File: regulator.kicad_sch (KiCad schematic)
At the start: 23 parts, among them U4 TPS63020DSJR, U5 MD53R33

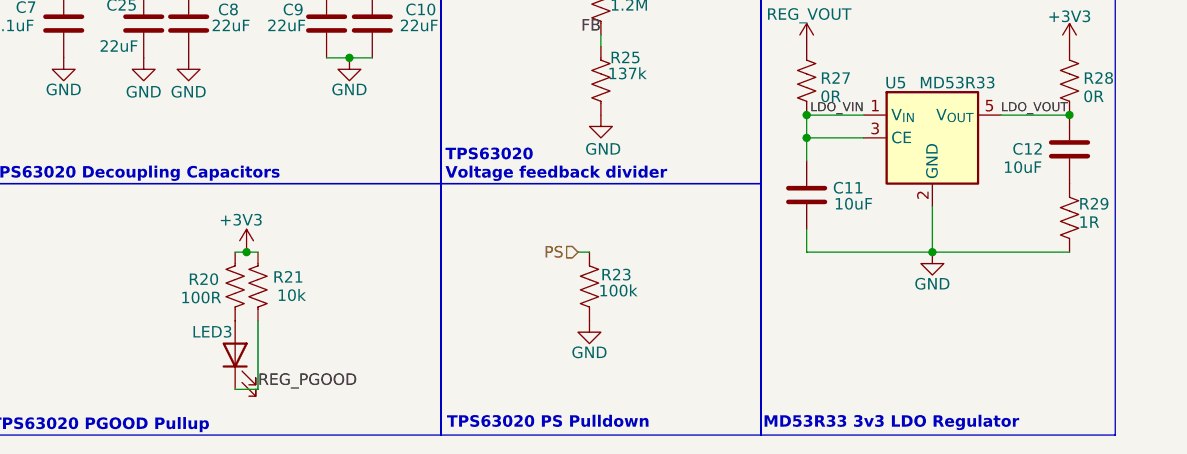
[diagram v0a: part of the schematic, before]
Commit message: Added labels and schematic PDF among other progress
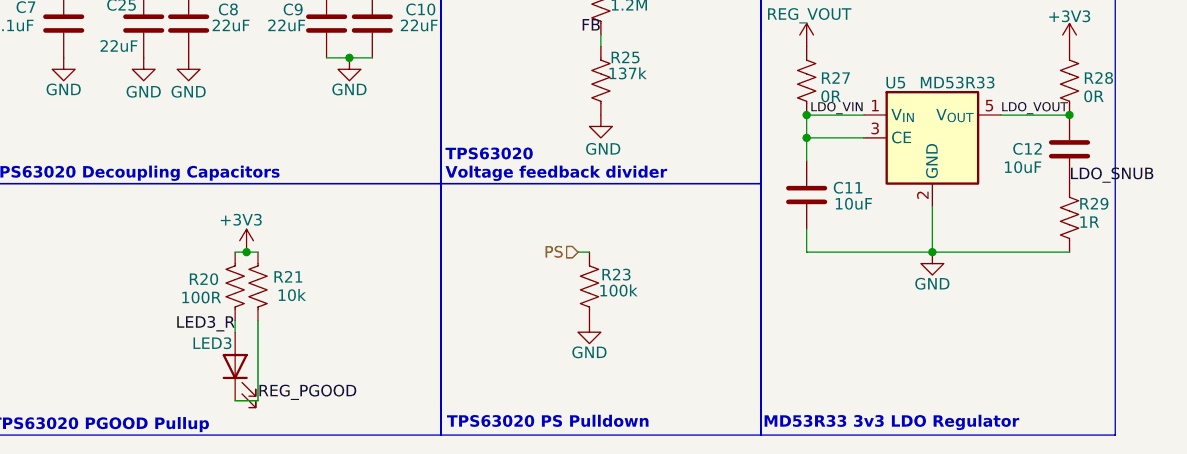
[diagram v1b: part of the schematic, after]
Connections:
- net LED3_R: now reaches LED3.2 (A), R20.1
- net LDO_SNUB: now reaches C12.2, R29.1
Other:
- moved on the sheet: LED3
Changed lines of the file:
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@@
 	(wire
 		(pts
-			(xy 110.49 162.56) (xy 107.95 162.56)
+			(xy 110.49 163.83) (xy 107.95 163.83)
 		)
 		(stroke
@@
 	(wire
 		(pts
+			(xy 110.49 154.94) (xy 110.49 163.83)
+		)
+		(stroke
+			(width 0)
+			(type default)
+		)
+	)
+	(wire
+		(pts
 			(xy 193.04 132.08) (xy 200.66 132.08)
 		)
@@
 	(wire
 		(pts
+			(xy 125.73 77.47) (xy 128.27 77.47)
+		)
+		(stroke
+			(width 0)
+			(type default)
+		)
+	)
+	(wire
+		(pts
 			(xy 185.42 147.32) (xy 200.66 147.32)
 		)
@@
 	(wire
 		(pts
-			(xy 125.73 77.47) (xy 128.27 77.47)
-		)
-		(stroke
-			(width 0)
-			(type default)
-		)
-	)
-	(wire
-		(pts
-			(xy 110.49 162.56) (xy 110.49 154.94)
-		)
-		(stroke
-			(width 0)
-			(type default)
-		)
-	)
-	(wire
-		(pts
 			(xy 109.22 147.32) (xy 110.49 147.32)
 		)
@@
 		(pts
 			(xy 97.79 118.11) (xy 102.7818 118.11)
+		)
+		(stroke
+			(width 0)
+			(type default)
+		)
+	)
+	(wire
+		(pts
+			(xy 107.95 156.21) (xy 107.95 154.94)
 		)
 		(stroke
@@
 	)
 	(label "REG_PGOOD"
-		(at 110.49 162.56 0)
+		(at 110.49 163.83 0)
 		(effects
 			(font
@@
 			)
 			(justify right bottom)
+		)
+	)
+	(label "LDO_SNUB"
+		(at 200.66 139.7 0)
+		(effects
+			(font
+				(size 1.27 1.27)
+			)
+			(justify left bottom)
 		)
 	)
@@
 				(size 1.27 1.27)
 				(thickness 0.1588)
+			)
+			(justify right bottom)
+		)
+	)
+	(label "LED3_R"
+		(at 107.95 156.21 180)
+		(effects
+			(font
+				(size 1.27 1.27)
 			)
 			(justify right bottom)
@@
 	(symbol
 		(lib_id "Device:LED")
-		(at 107.95 158.75 90)
+		(at 107.95 160.02 90)
 		(unit 1)
 		(body_style 1)
@@
 		(dnp no)
 		(property "Reference" "LED3"
-			(at 105.41 156.21 90)
+			(at 105.41 157.48 90)
 			(show_name no)
 			(do_not_autoplace no)
@@
 		)
 		(property "Value" "PGOOD"
-			(at 104.14 160.3375 0)
+			(at 104.14 161.6075 0)
 			(hide yes)
 			(show_name no)
@@
 		)
 		(property "Footprint" "LED_SMD:LED_0603_1608Metric"
-			(at 107.95 158.75 0)
+			(at 107.95 160.02 0)
 			(hide yes)
 			(show_name no)
@@
 		)
 		(property "Datasheet" ""
-			(at 107.95 158.75 0)
+			(at 107.95 160.02 0)
 			(hide yes)
 			(show_name no)
@@
 		)
 		(property "Description" "Light emitting diode"
-			(at 107.95 158.75 0)
+			(at 107.95 160.02 0)
 			(hide yes)
 			(show_name no)
@@
 		)
 		(property "Sim.Pins" "1=K 2=A"
-			(at 107.95 158.75 0)
+			(at 107.95 160.02 0)
 			(hide yes)
 			(show_name no)
@@
 		)
 		(property "MFR#" ""
-			(at 107.95 158.75 0)
+			(at 107.95 160.02 0)
 			(hide yes)
 			(show_name no)
@@
 		)
 		(property "Package" "0603"
-			(at 107.95 158.75 0)
+			(at 107.95 160.02 0)
 			(hide yes)
 			(show_name no)
@@
 		)
 		(property "LCSC#" "C2286"
-			(at 107.95 158.75 90)
-			(hide yes)
-			(show_name no)
+			(at 107.95 160.02 90)
+			(hide yes)
+			(show_name no)

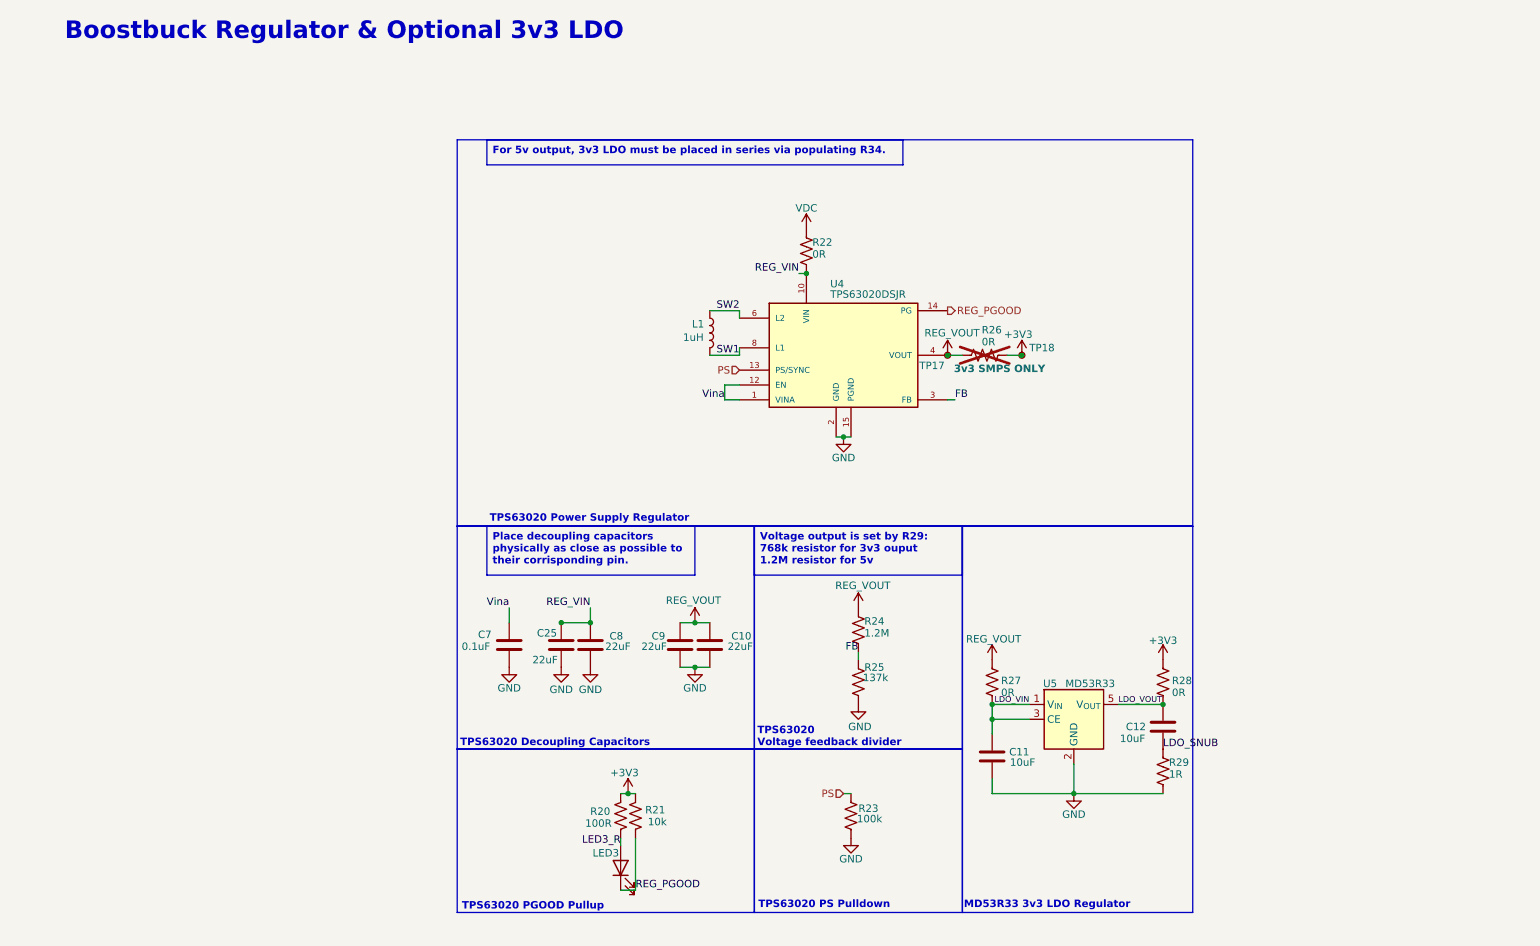
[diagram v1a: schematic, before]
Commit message: Added testpoints
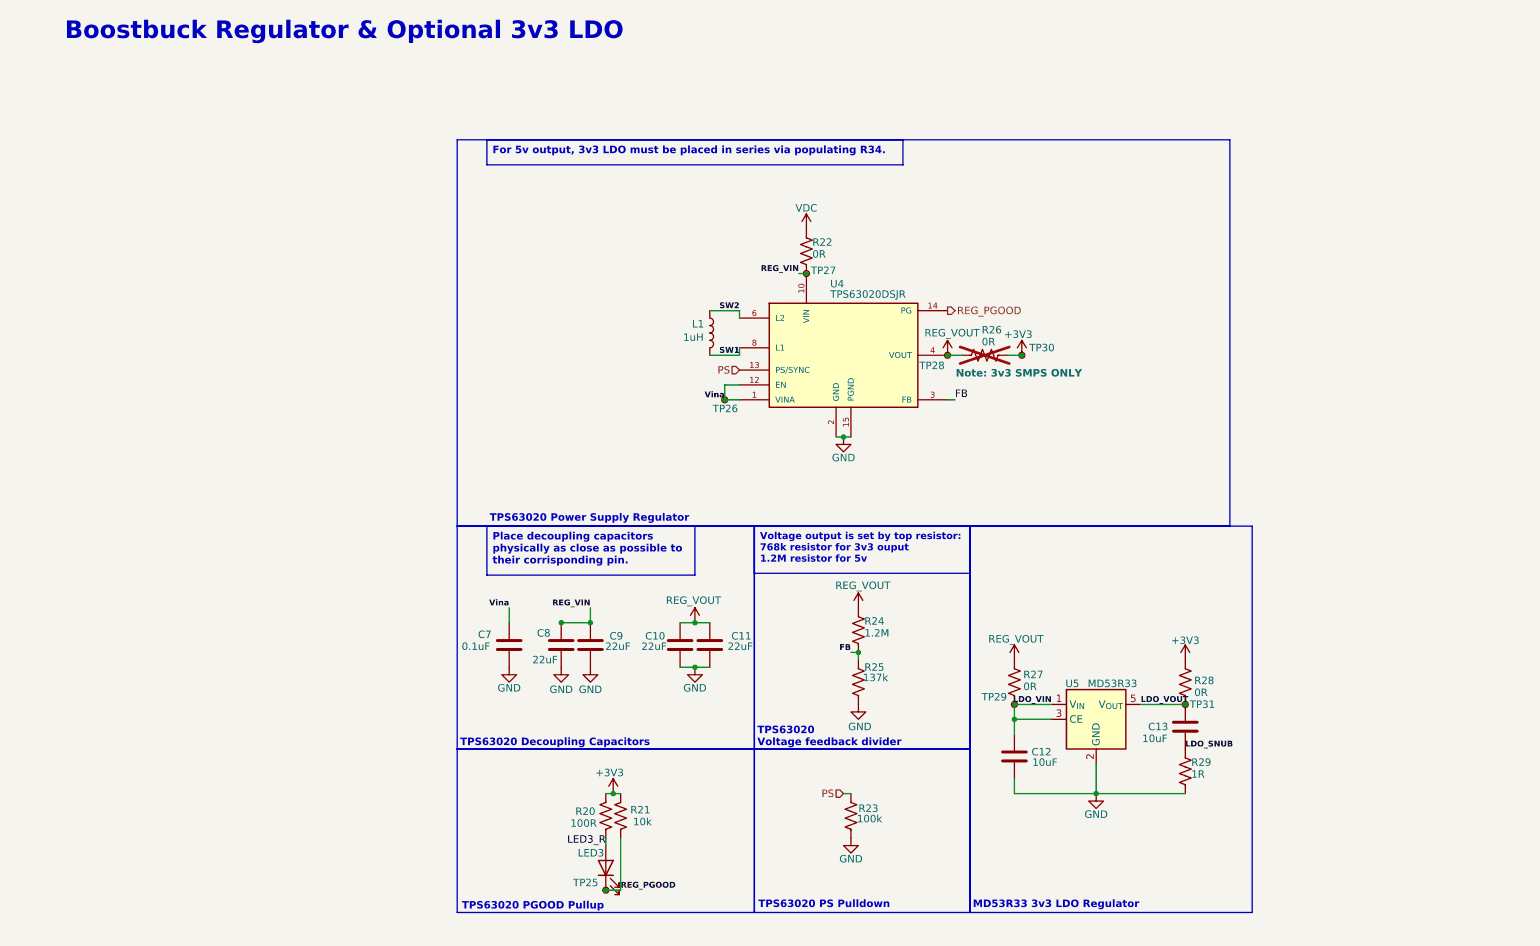
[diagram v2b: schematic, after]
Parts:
- added TP25: REG_PGOOD, symbol Connector:TestPoint_Small
- added TP26: REG_Vina, symbol Connector:TestPoint_Small
- added TP27: REG_VIN, symbol Connector:TestPoint_Small
- added TP29: LDO_VIN, symbol Connector:TestPoint_Small
- added TP31: LDO_VOUT, symbol Connector:TestPoint_Small
- R26: Label 3v3 SMPS ONLY -> (none); Note (none) -> 3v3 SMPS ONLY
- renumbered C9 to C10, C10 to C11, C11 to C12, C12 to C13, C25 to C8, C8 to C9, TP17 to TP28, TP18 to TP30
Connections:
- net LDO_VIN: now also TP29.1
- net LDO_VOUT: now also TP31.1
- net REG_PGOOD: now also TP25.1
- net REG_VIN: now also TP27.1
- net Vina: now also TP26.1
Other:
- moved on the sheet: C12, C13, LED3, R20, R21, R27, R28, R29, U5

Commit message: Configured Varients
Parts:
- renumbered R20 to R21, R21 to R22, R22 to R23, R23 to R24, R24 to R25, R25 to R26, R26 to R27, R27 to R28, R28 to R29, R29 to R30
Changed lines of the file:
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@@
 		(in_pos_files yes)
 		(dnp no)
-		(property "Reference" "R22"
+		(property "Reference" "R23"
 			(at 140.716 53.086 0)
 			(show_name no)
@@
 			(project "power_module"
 				(path "/33e2b92e-f705-4be7-96f4-57092b8ec1ea/8030bb5b-b463-45e7-87db-4ab635727d1f"
-					(reference "R22")
+					(reference "R23")
 					(unit 1)
 				)
@@
 		(in_pos_files yes)
 		(dnp yes)
-		(property "Reference" "R26"
+		(property "Reference" "R27"
 			(at 169.672 68.072 90)
 			(show_name no)
@@
 			(project "power_module"
 				(path "/33e2b92e-f705-4be7-96f4-57092b8ec1ea/8030bb5b-b463-45e7-87db-4ab635727d1f"
-					(reference "R26")
+					(reference "R27")
 					(unit 1)
+					(variant
+						(name "3v3")
+						(dnp no)
+					)
+					(variant
+						(name "3v3 Dumb")
+						(dnp no)
+					)
 				)
 			)
@@
 		(in_pos_files yes)
 		(dnp no)
-		(property "Reference" "R27"
+		(property "Reference" "R28"
 			(at 176.784 127 0)
 			(show_name no)
@@
 			(project "power_module"
 				(path "/33e2b92e-f705-4be7-96f4-57092b8ec1ea/8030bb5b-b463-45e7-87db-4ab635727d1f"
-					(reference "R27")
+					(reference "R28")
 					(unit 1)
+					(variant
+						(name "3v3")
+						(dnp yes)
+						(exclude_from_sim yes)
+					)
+					(variant
+						(name "3v3 Dumb")
+						(dnp yes)
+					)
 				)
 			)
@@
 					(reference "C13")
 					(unit 1)
+					(variant
+						(name "3v3")
+						(dnp yes)
+					)
+					(variant
+						(name "3v3 Dumb")
+						(dnp yes)
+					)
 				)
 			)
@@
 		(in_pos_files yes)
 		(dnp no)
-		(property "Reference" "R20"
+		(property "Reference" "R21"
 			(at 103.632 150.368 0)
 			(show_name no)
@@
 			(project "power_module"
 				(path "/33e2b92e-f705-4be7-96f4-57092b8ec1ea/8030bb5b-b463-45e7-87db-4ab635727d1f"
-					(reference "R20")
+					(reference "R21")
 					(unit 1)
 				)
@@
 		(in_pos_files yes)
 		(dnp no)
-		(property "Reference" "R21"
+		(property "Reference" "R22"
 			(at 113.03 150.114 0)
 			(show_name no)
@@
 			(project "power_module"
 				(path "/33e2b92e-f705-4be7-96f4-57092b8ec1ea/8030bb5b-b463-45e7-87db-4ab635727d1f"
-					(reference "R21")
+					(reference "R22")
 					(unit 1)
 				)
@@
 					(reference "C12")
 					(unit 1)
+					(variant
+						(name "3v3")
+						(dnp yes)
+					)
+					(variant
+						(name "3v3 Dumb")
+						(dnp yes)
+					)
 				)
 			)
@@
 		(in_pos_files yes)
 		(dnp no)
-		(property "Reference" "R29"
+		(property "Reference" "R30"
 			(at 205.486 141.986 0)
 			(show_name no)
@@
 			(project "power_module"
 				(path "/33e2b92e-f705-4be7-96f4-57092b8ec1ea/8030bb5b-b463-45e7-87db-4ab635727d1f"
-					(reference "R29")
+					(reference "R30")
 					(unit 1)
+					(variant
+						(name "3v3")
+						(dnp yes)
+					)
+					(variant
+						(name "3v3 Dumb")
+						(dnp yes)
+					)
 				)
 			)
@@
 					(reference "U5")
 					(unit 1)
+					(variant
+						(name "3v3")
+						(dnp yes)
+					)
+					(variant
+						(name "3v3 Dumb")
+						(dnp yes)
+					)
 				)
 			)
@@
 		(in_pos_files yes)
 		(dnp no)
-		(property "Reference" "R23"
+		(property "Reference" "R24"
 			(at 148.59 149.86 0)
 			(show_name no)
@@
 			(project "power_module"
 				(path "/33e2b92e-f705-4be7-96f4-57092b8ec1ea/8030bb5b-b463-45e7-87db-4ab635727d1f"
-					(reference "R23")
+					(reference "R24")
 					(unit 1)
 				)
@@
 		(in_pos_files yes)
 		(dnp no)
-		(property "Reference" "R25"
+		(property "Reference" "R26"
 			(at 149.606 125.73 0)
 			(show_name no)
@@
 			(project "power_module"
 				(path "/33e2b92e-f705-4be7-96f4-57092b8ec1ea/8030bb5b-b463-45e7-87db-4ab635727d1f"
-					(reference "R25")
+					(reference "R26")
 					(unit 1)
 				)
@@
 		(in_pos_files yes)
 		(dnp no)
-		(property "Reference" "R24"
+		(property "Reference" "R25"
 			(at 149.606 117.856 0)
 			(show_name no)
@@
 			(project "power_module"
 				(path "/33e2b92e-f705-4be7-96f4-57092b8ec1ea/8030bb5b-b463-45e7-87db-4ab635727d1f"
-					(reference "R24")
+					(reference "R25")
 					(unit 1)
+					(variant
+						(name "3v3")
+						(field
+							(name "Value")
+							(value "768k")
+						)
+					)
+					(variant
+						(name "3v3 Dumb")
+						(field
+							(name "Value")
+							(value "768k")
+						)
+					)
 				)
 			)
@@
 		(in_pos_files yes)
 		(dnp no)
-		(property "Reference" "R28"
+		(property "Reference" "R29"
 			(at 205.994 128.016 0)
 			(show_name no)
@@
 			(project "power_module"
 				(path "/33e2b92e-f705-4be7-96f4-57092b8ec1ea/8030bb5b-b463-45e7-87db-4ab635727d1f"
-					(reference "R28")
+					(reference "R29")
 					(unit 1)
+					(variant
+						(name "3v3")
+						(dnp yes)
+					)
+					(variant
+						(name "3v3 Dumb")
+						(dnp yes)
+					)
 				)
 			)
